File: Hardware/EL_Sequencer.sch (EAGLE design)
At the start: 109 parts, among them J1 Battery, J10 M02-JST-2MM-SMT, J11 M02-JST-2MM-SMT, J2 DC-OUTPUT, J3 AC-INPUT, J4 M02-JST-2MM-SMT, J5 M02-JST-2MM-SMT, J6 M02-JST-2MM-SMT, J7 M02-JST-2MM-SMT, J8 M02-JST-2MM-SMT, J9 M02-JST-2MM-SMT, U1 LM317, U10 Z0103MN, U11 Z0103MN, U12 Z0103MN, U13 MOC3063S, U14 MOC3063S, U15 MOC3063S, U16 MOC3063S, U17 Z0103MN, U18 Z0103MN, U19 Z0103MN, U2 MIC5219 3.3V, U20 Z0103MN, U3 ATMEGA328P, U4-DNP XBEE HEADER, U5 MOC3063S, U6 MOC3063S, U7 MOC3063S, U8 MOC3063S, U9 Z0103MN, Y1 8MHZ

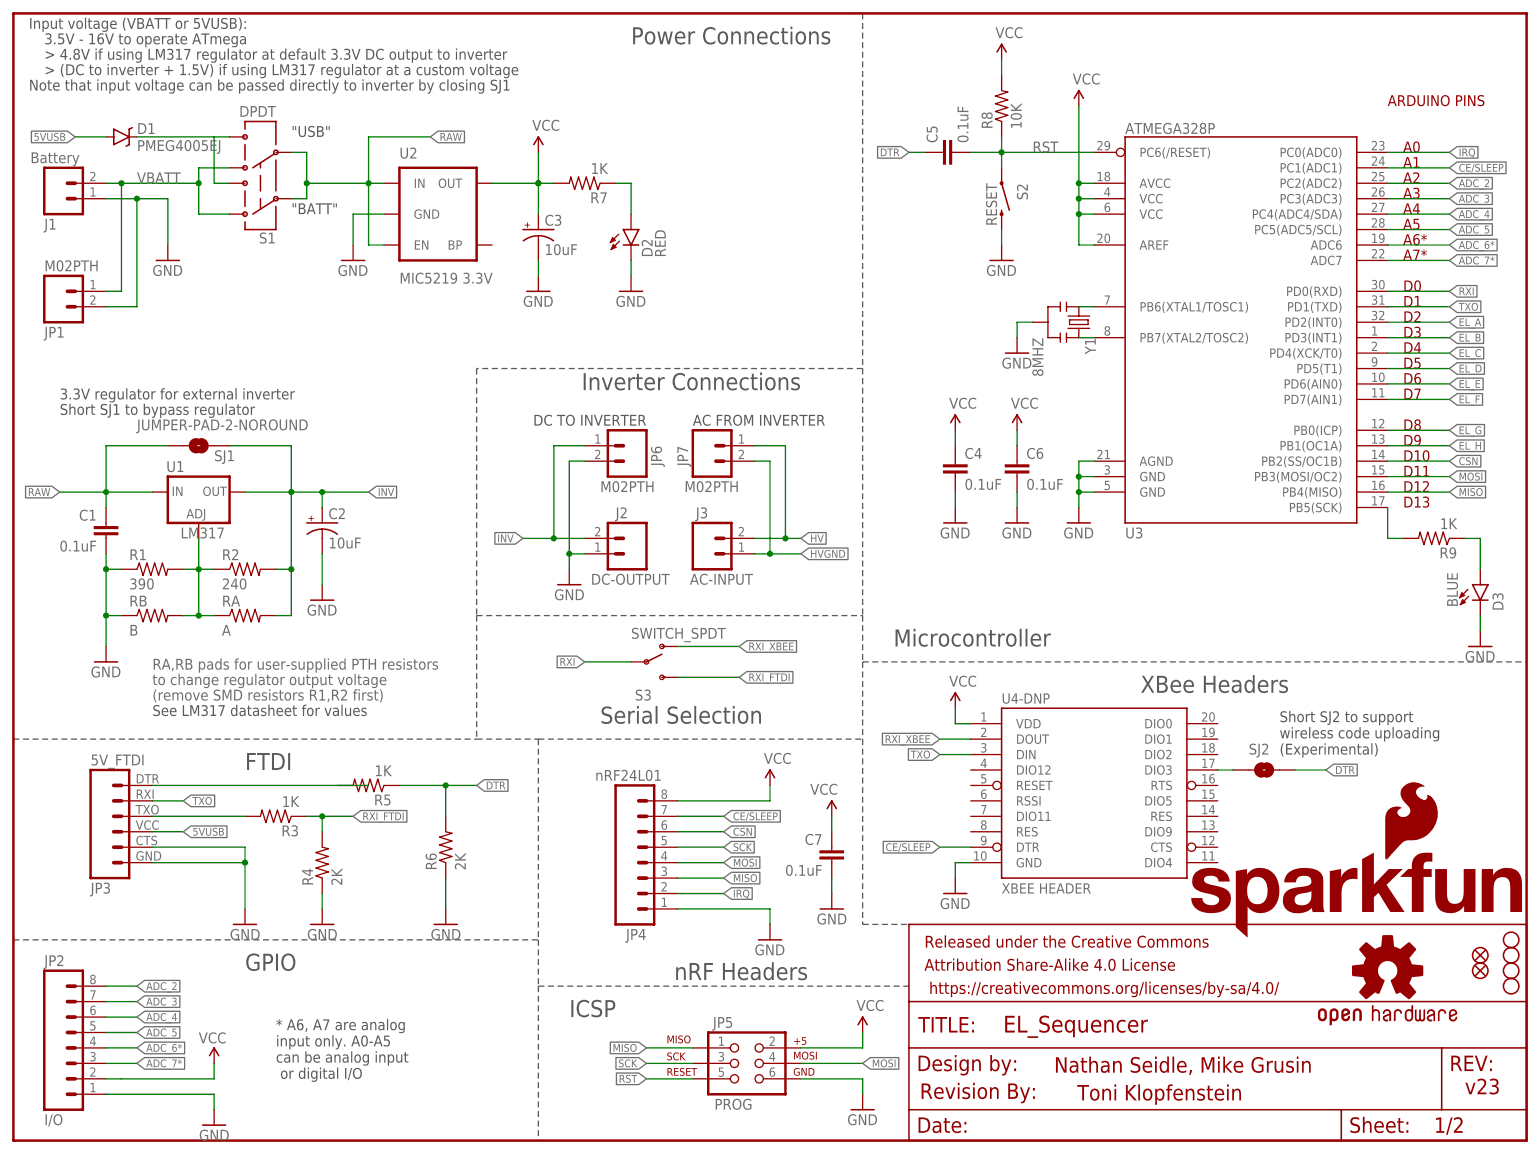
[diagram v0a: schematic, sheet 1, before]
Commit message: Fixing issues from QC check
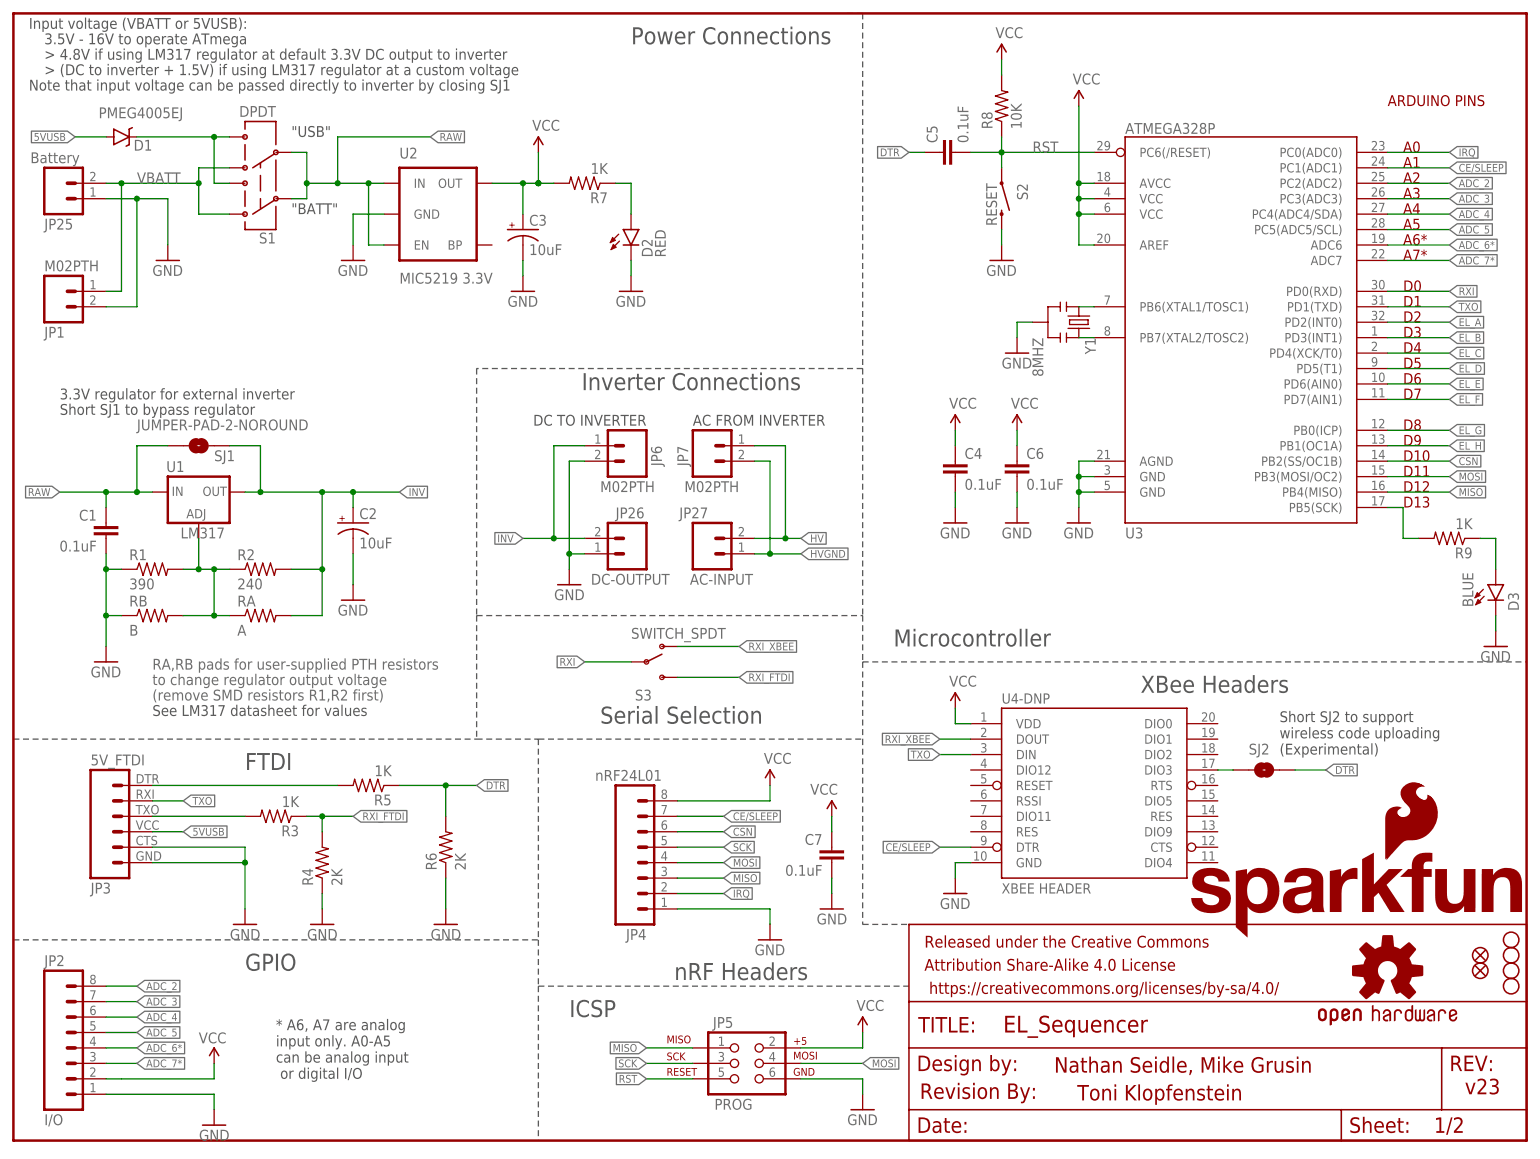
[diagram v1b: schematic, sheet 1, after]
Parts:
- renumbered J1 to JP25, J10 to JP22, J11 to JP21, J2 to JP26, J3 to JP27, J4 to JP17, J5 to JP18, J6 to JP19, J7 to JP20, J8 to JP24, J9 to JP23
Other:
- moved on the sheet: C2, C3, D3, R2, R9, RA
